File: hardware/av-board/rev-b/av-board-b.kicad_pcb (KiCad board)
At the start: 4 copper layers, 94.6 x 69.4 mm, 234 parts, among them J1 RCA Y, J10 2x20 socket, J11 XIAO 5V..D7, J12 XIAO D0..D6, J13 SPDIF, J2 RCA Pb, J3 RCA Pr, J4 RCA L, J5 RCA R, J6 HDMI-001, J7 SYNC, J8 VGA, J9 2x20 socket, Q1 2N7002, Q2 2N7002, SW1 TS-1187A-B-A-B, SW2 TS-1187A-B-A-B, U1 ADV7181DBCPZ-RL, U10 TPD4E05U06DQAR, U12 TPS7A2045PDBVR, U13 SN74LVC1GU04DBVR, U14 SN74LVC1G04DBVR, U15 SN74LVC1G04DBVR, U19 TPD4E05U06DQAR, U2 ADV7511KSTZ, U20 TPD4E05U06DQAR, U21 SN74LVC2G17DBVR, U22 SN74LVC8T245PWR, U23 SN74AVC4T245PWR, U3 PCM1808PWR, U4 TLV62569DBVR, U5 TPS7A7001DDAR, U6 TPS7A7001DDAR, U7 TPS7A7001DDAR, U8 TPD4E05U06DQAR, U9 TPD4E05U06DQAR, Y1 28.63636MHz 20pF

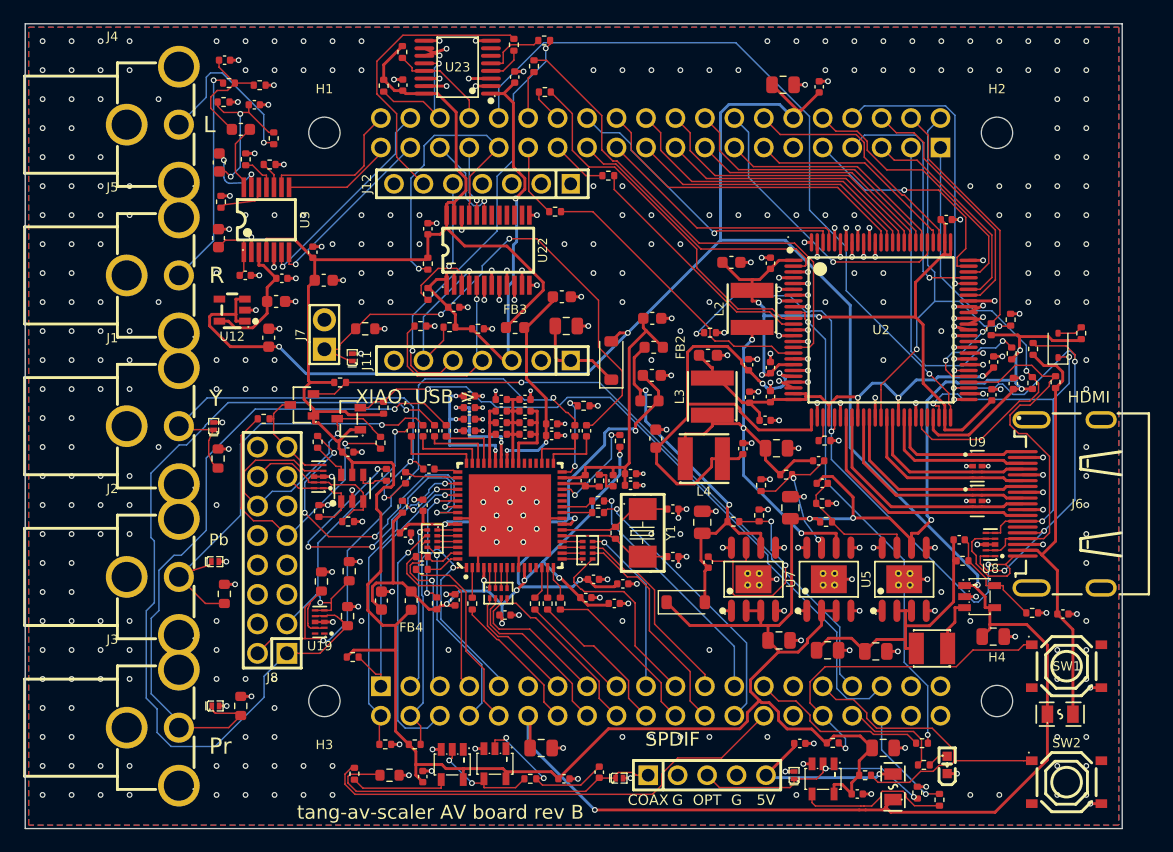
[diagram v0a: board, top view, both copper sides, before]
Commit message: AV boards: silkscreen to JLCPCB's limits; the XIAO's way in printed on rev C
JLCPCB's silkscreen limits (its capabilities page): lines and strokes 0.15 mm
at least, text 1 mm high with a 1:6 stroke, 0.15 mm from pads.

- kit/pcbkit.py: designators and pin labels 1 mm (were 0.8 and 0.9 mm), every
  text's stroke 1:6 of its height; designators clear of the other parts'
  bodies, tried at 40 places beside their part before its own body.
  silk_tidy(): the parts' own silkscreen widened to 0.15 mm and cut back where
  it came within 0.15 mm of a pad, past the board's edge, under a text or onto
  another part's (the bigger parts first); EasyEDA's 0.12 mm pin 1 dots (too
  small to print) taken out, small marks moved clear. A second run changes
  nothing.
- Rev B, C-A, C-B: the silkscreen pass run again (--silk): only the silkscreen
  Gerbers changed. DRC: no silkscreen warnings (were 56, 63, 54); designators
  shown 36, 51, 45 (were 35, 41, 33). The trimmed footprints now differ from
  the library (DRC's lib_footprint_mismatch, noted in the reviews).
- Rev B: "XIAO, USB >" by J12 (by J11 no place was clear: it lay over copper).
- Rev C: the XIAO's way in printed beside J12, "XIAO, USB >" reading down to
  its USB-C's end (that of D0 and 5V, the sockets' pin 1, at the bottom edge);
  kit SILK_NEAR entries may carry an angle (the label beside the part).

Co-Authored-By: Claude Opus 5.5 <noreply@anthropic.com>
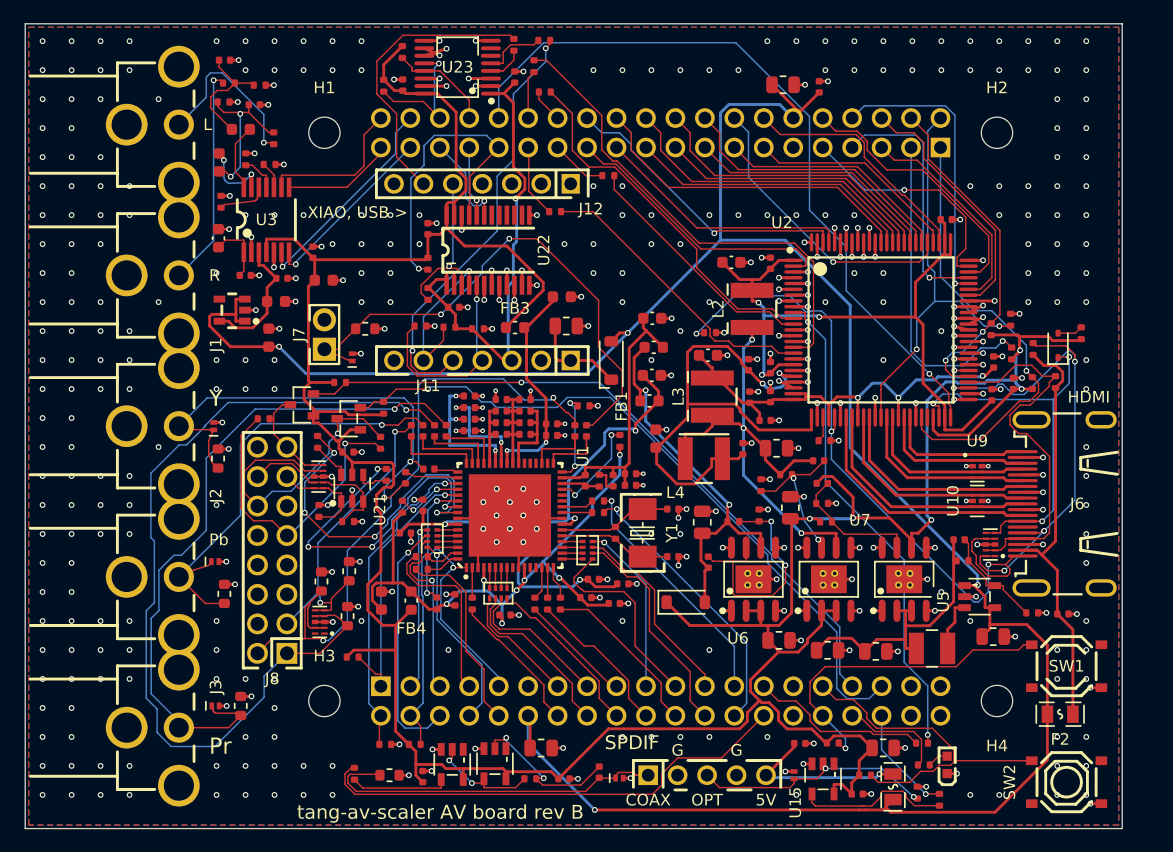
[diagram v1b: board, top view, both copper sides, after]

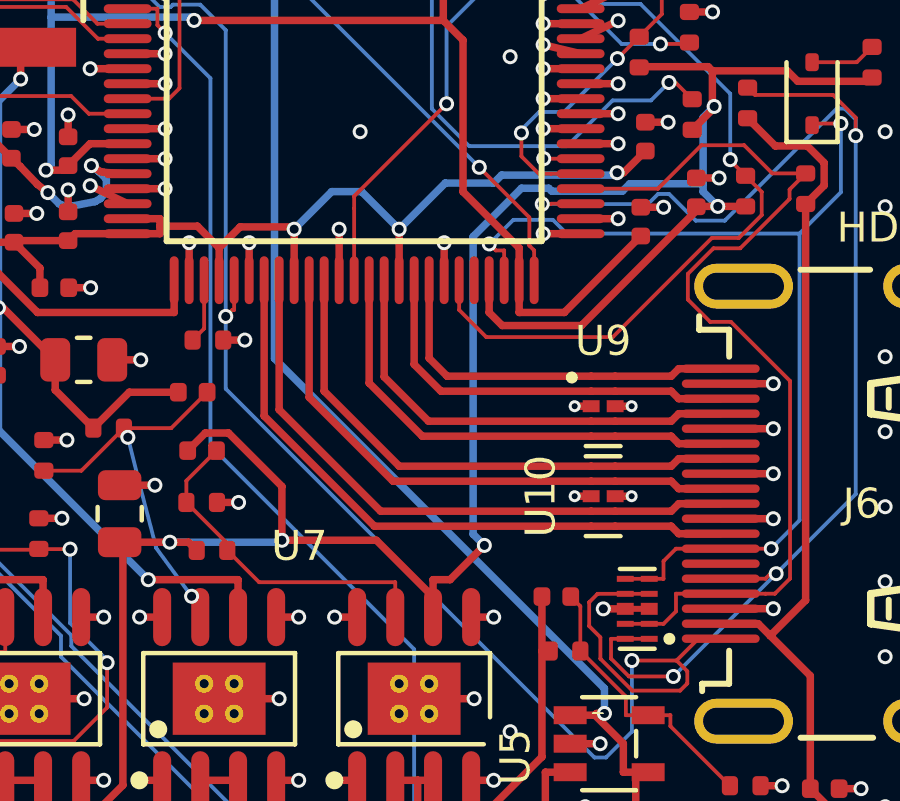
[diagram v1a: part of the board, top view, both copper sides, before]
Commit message: AV boards: the TMDS keep-outs from the kit for every revision; rev B's 3V3 off TMDS_CK
The keep-outs along the TMDS pairs (TI SPRAAR7 3.1-3.3: other lines 30 mil off, 1.5 W from plane
voids; 3.14: the planes voided under 60 % of the ESD arrays' pads) were C-B's own; now
kit/tmds_layout.py makes them for any revision on TMDSLayout:
- tmds_keepouts(): rule areas on F.Cu outside the outermost line, inside the innermost and
  between the pairs, each following the lines round their corners, from the corner (or, with
  TMDS_KEEP_OUT, from past the chip's 0.25 in break-out along the first leg) to where the pairs
  close up before the arrays (unspread: TMDS_KEEP_END, 1 mm, before the arrays' pads, clear of
  their ground vias between the pairs); In1 and In2 voided under the arrays' TMDS pads. Worked
  out from the locked lines on the board, so the same on a routed board as on a new one.
- pcbkit: a keepouts() hook after the fanout; rule areas named (KEEPOUT_NAMES); --keepouts
  renews a routed board's (the old ones off, the new on, the copper they hold out taken up,
  locked copper there an error), --complete then routes those connections again.

Rev B (the audit, kit/hdmi_audit.py rev-b): a 3V3 track and via stood 0.22 and 0.26 mm from
TMDS_CK_N (the via's antipad 0.11 mm from it in In1), and nothing was voided under the arrays.
With the keep-outs renewed on the routed board, 3V3 is routed again round them (crossing under
the pairs on B.Cu); the rest of the route as it was. DRC 0 errors, 0 unconnected; the decoupling
and analog-isolation reports unchanged. Left: the pairs 0.75 mm (3 W) apart on the 2.9 mm of
TMDS_CK that lies past the break-outs, against 3.4's 0.76: too short a run to spread.

C-B: its keep-outs from the kit (its lanes' AC capacitors' voids its own): the outer strip one
piece round TMDS_CK's corner (it was two, a sliver open between them); renewed on the routed
board, nothing in the way. The review's DP_OE finding is C95's pad (DP_OE's 100 nF, static)
0.74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
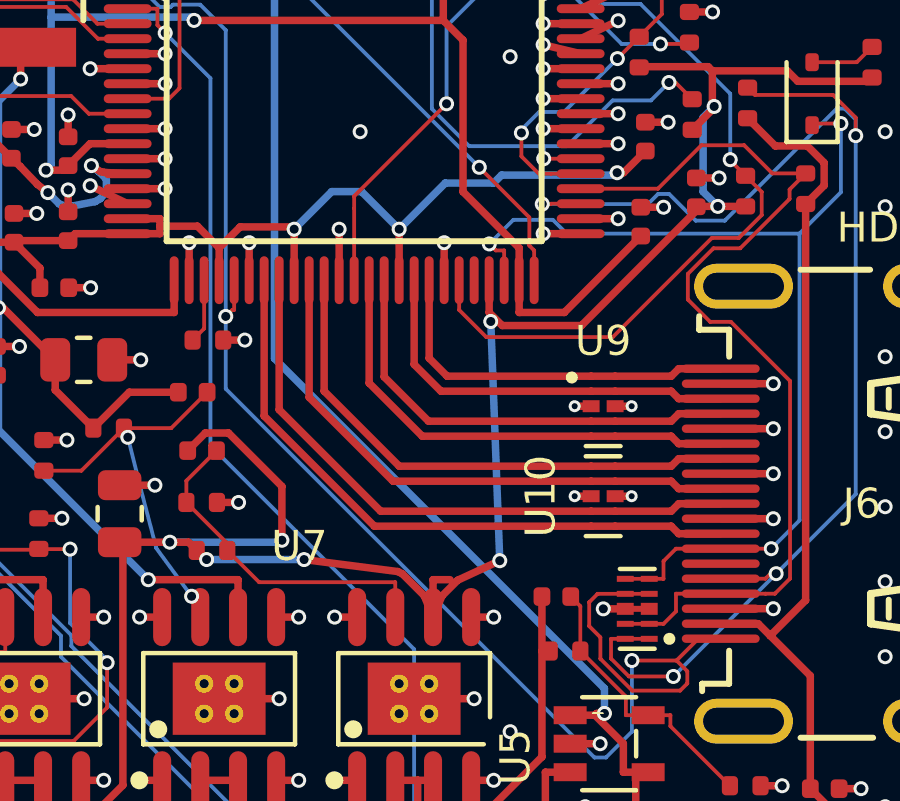
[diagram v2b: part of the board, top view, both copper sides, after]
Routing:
- net 3V3: track 290.8 -> 284.3 mm, vias 5 -> 8
